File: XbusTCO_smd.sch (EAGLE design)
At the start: 80 parts, among them IC1 74HC4515D, IC2 PIC16F628P, IC3 MAX481CSA, IC4 78L05SMD, X1 1751264

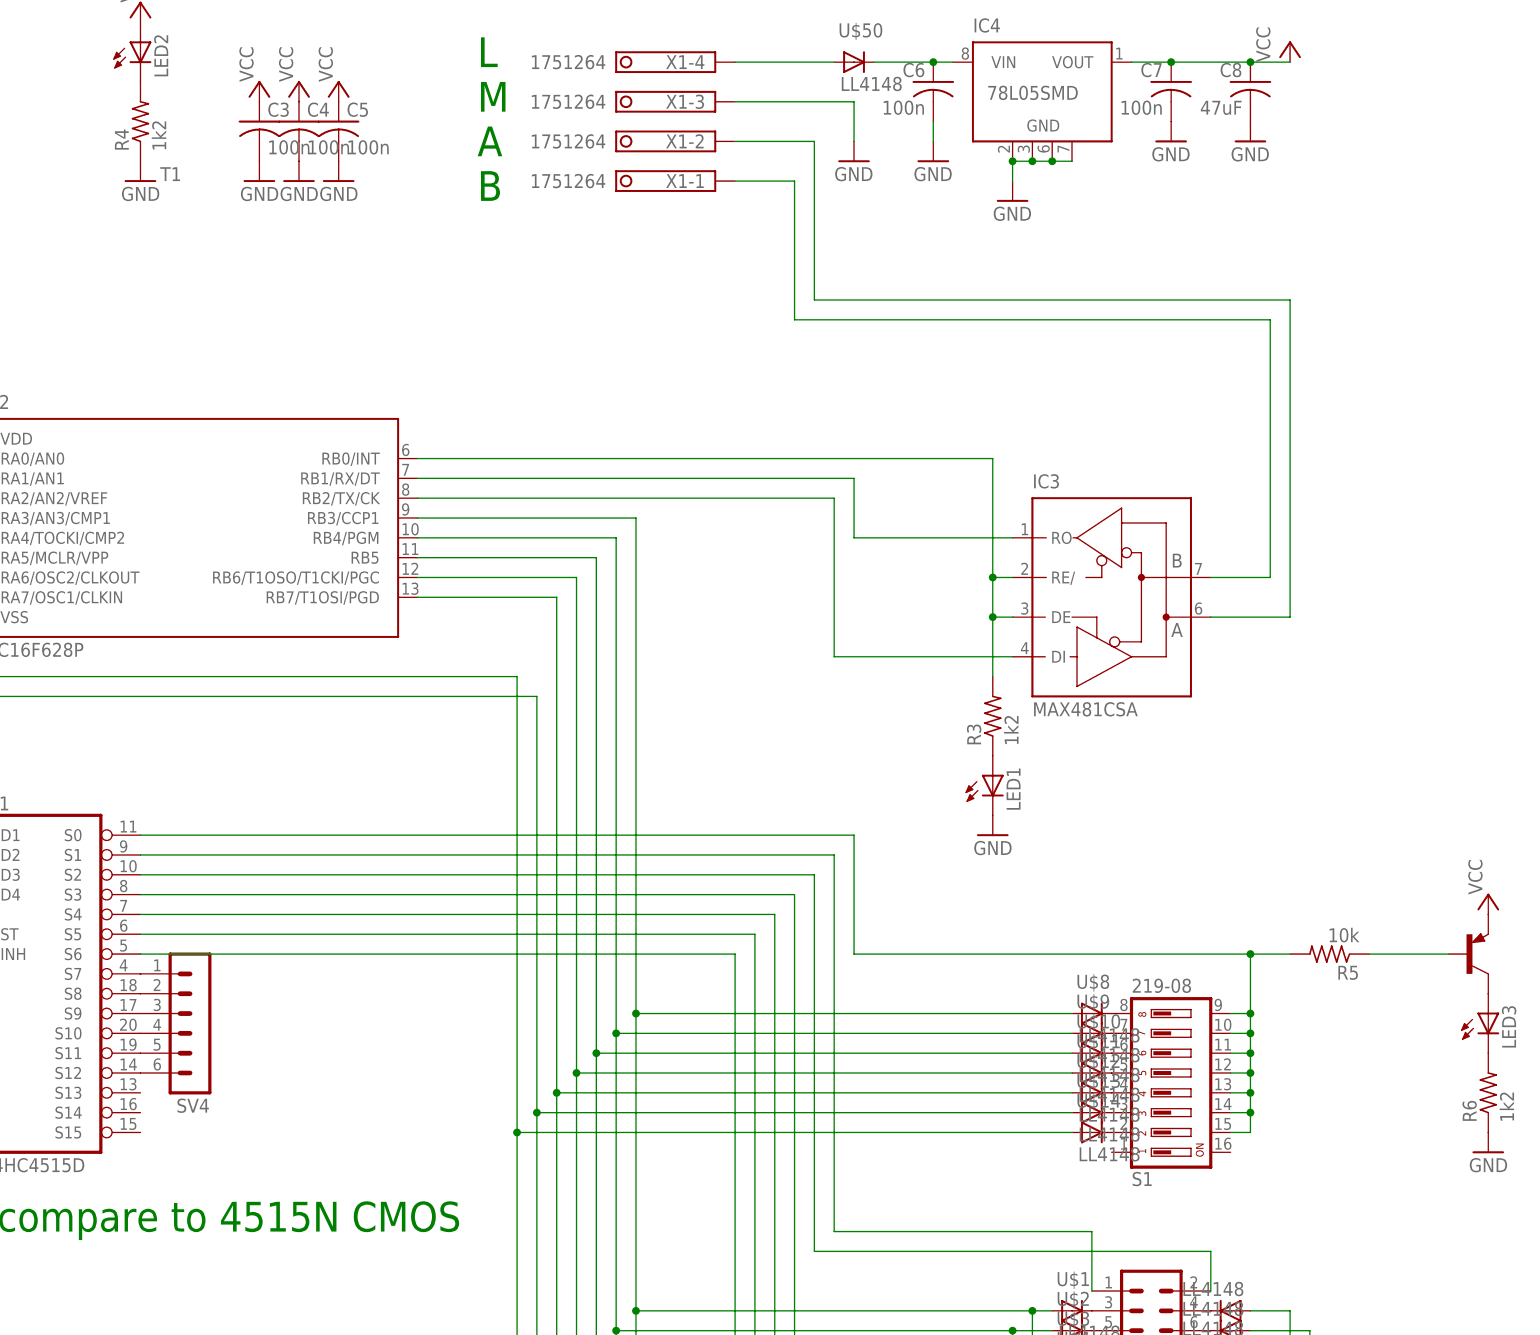
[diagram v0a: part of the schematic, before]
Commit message: Updated DIL switch pinout.
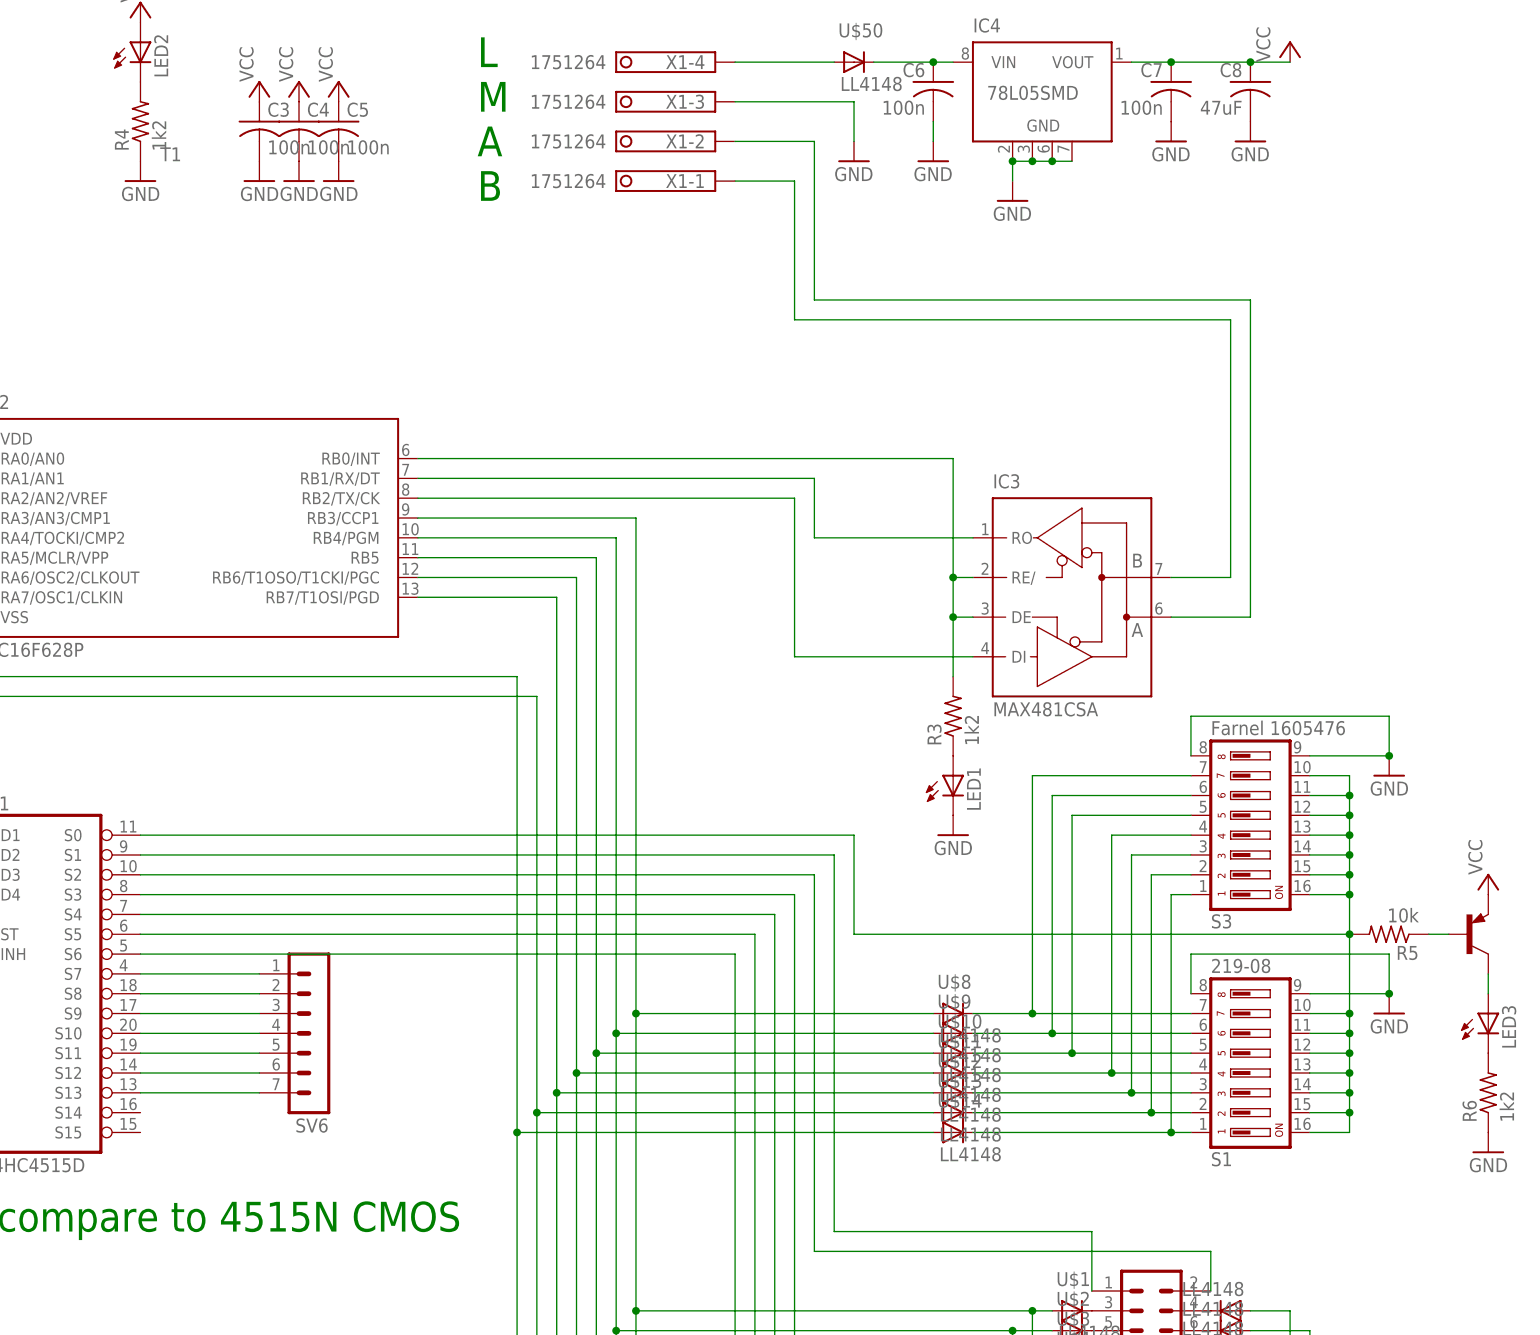
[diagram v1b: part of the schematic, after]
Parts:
- removed SV4: (no value), con-lstb:MA06-1
- added S3: Farnel 1605476, switch-dil:219-08J
- added SV6: (no value), con-lstb:MA07-1
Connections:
- new net N$88: IC1A.S13, SV6.7
- net GND: now also S1.8, S1.9, S3.8, S3.9
- net N$30: now also S1.16, S3.10, S3.11, S3.12, S3.13, S3.14, S3.15, S3.16; no longer S1.9
- net N$31: now also S1.7, S3.7; no longer S1.8
- net N$32: now also S1.6, S3.6; no longer S1.7
- net N$33: now also S1.5, S3.5; no longer S1.6
- net N$34: now also S1.4, S3.4; no longer S1.5
- net N$35: now also S1.3, S3.3; no longer S1.4
- net N$36: now also S1.2, S3.2; no longer S1.3
- net N$37: now also S1.1, S3.1; no longer S1.2
- net N$82: now also SV6.1; no longer SV4.1
- net N$83: now also SV6.2; no longer SV4.2
- net N$84: now also SV6.3; no longer SV4.3
- net N$85: now also SV6.4; no longer SV4.4
- net N$86: now also SV6.5; no longer SV4.5
- net N$87: now also SV6.6; no longer SV4.6
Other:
- moved on the sheet: IC3, LED1, R3, R5, S1, T1, U$10, U$11, U$12, U$13, U$14, U$8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

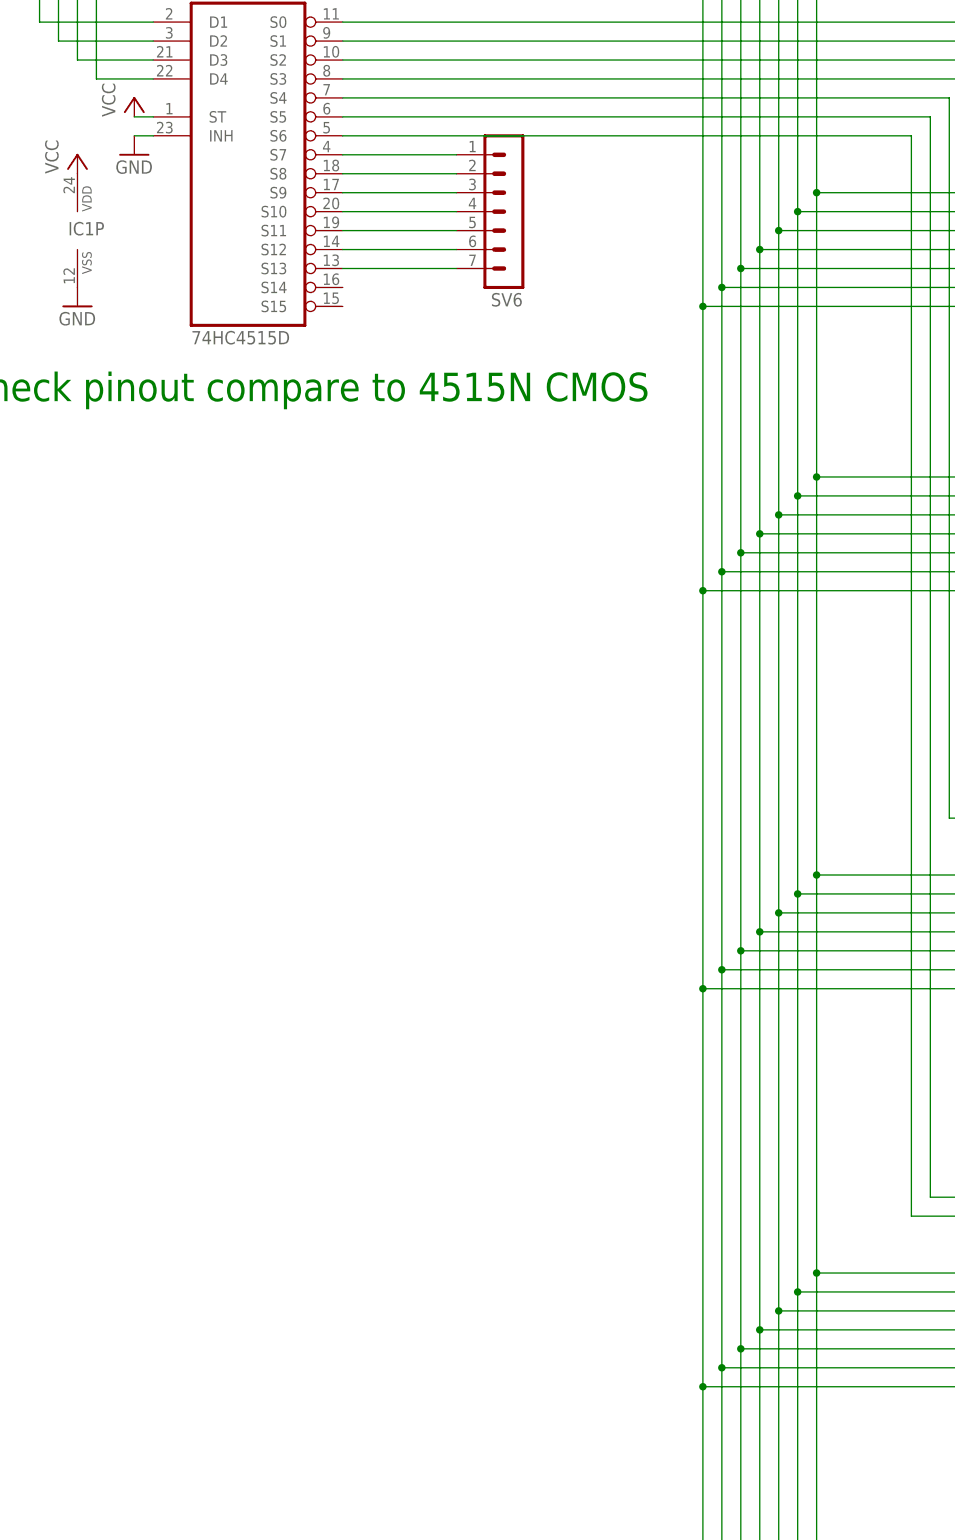
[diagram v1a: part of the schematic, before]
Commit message: Added 2 more connectors.
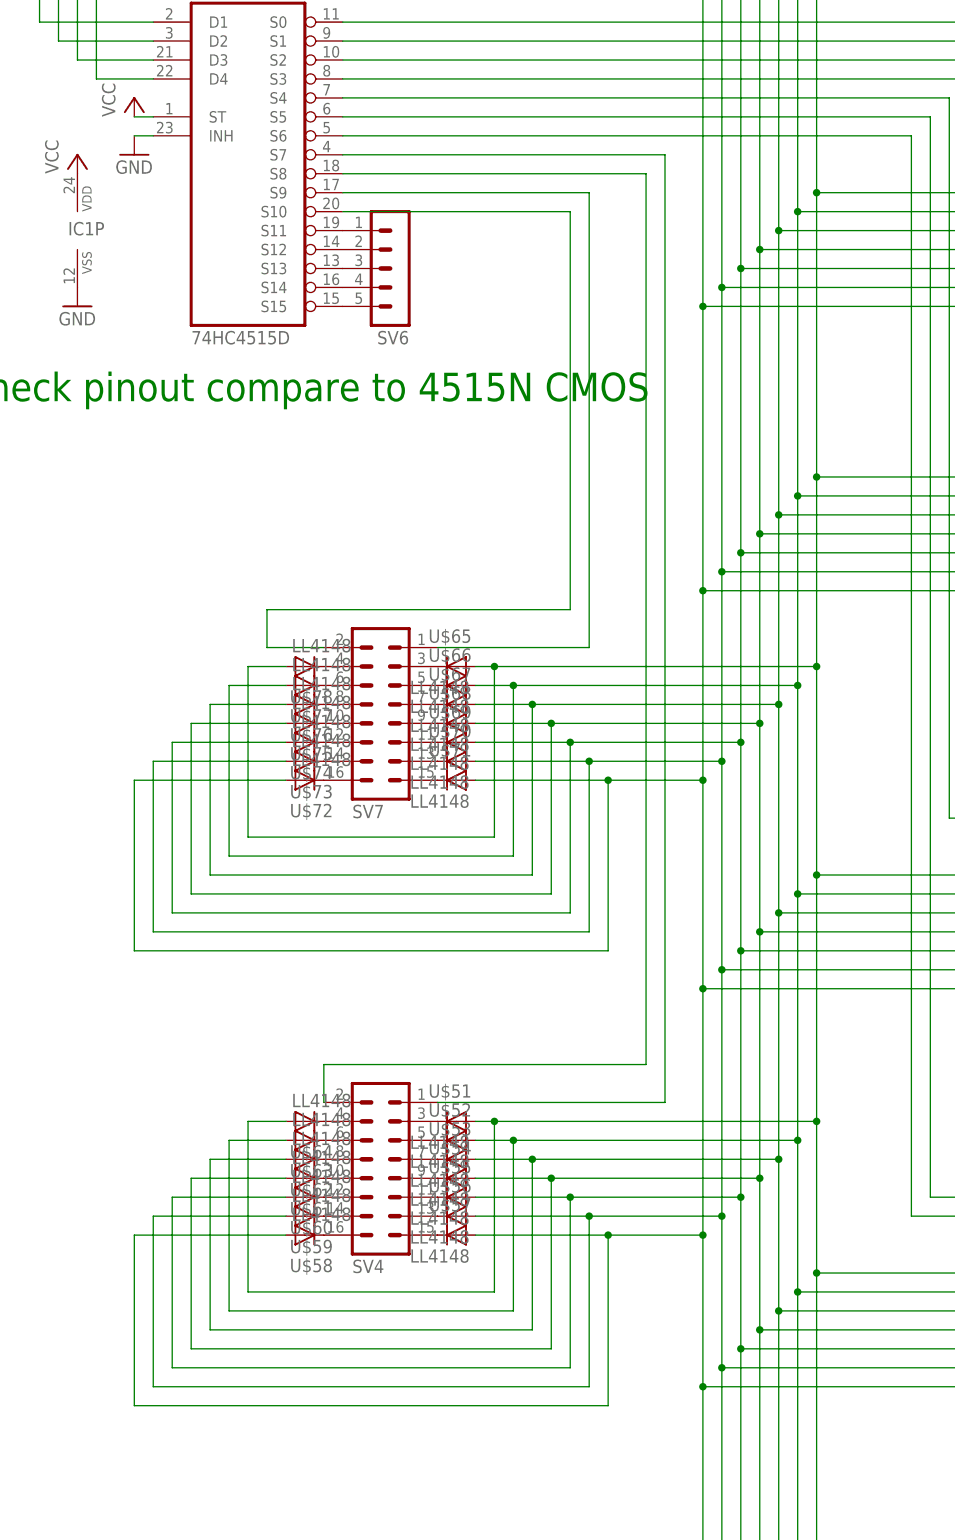
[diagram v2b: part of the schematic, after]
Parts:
- added SV4, SV7: (no value), con-lstb:MA08-2W
- added U$51, U$52, U$53, U$54, U$55, U$56, U$57, U$58, U$59, U$60, U$61, U$62, U$63, U$64, U$65, U$66, U$67, U$68, U$69, U$70, U$71, U$72, U$73, U$74, U$75, U$76, U$77, U$78: LL4148, LL4148:LL4148
- SV6: device con-lstb:MA07-1 -> con-lstb:MA05-1
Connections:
- new net N$100: SV4.7, U$53.C
- new net N$101: SV4.9, U$54.C
- new net N$102: SV4.11, U$55.C
- new net N$103: SV4.13, U$56.C
- new net N$104: SV4.15, U$57.C
- new net N$105: SV4.16, U$58.C
- new net N$106: SV4.14, U$59.C
- new net N$107: SV4.12, U$60.C
- new net N$108: SV4.10, U$61.C
- new net N$109: SV4.8, U$62.C
- new net N$110: SV4.6, U$63.C
- new net N$111: SV4.4, U$64.C
- new net N$112: SV7.7, U$67.C
- new net N$113: SV7.9, U$68.C
- new net N$114: SV7.11, U$69.C
- new net N$115: SV7.13, U$70.C
- new net N$116: SV7.15, U$71.C
- new net N$117: SV7.16, U$72.C
- new net N$118: SV7.14, U$73.C
- new net N$119: SV7.12, U$74.C
- new net N$120: SV7.10, U$75.C
- new net N$121: SV7.8, U$76.C
- new net N$122: SV7.6, U$77.C
- new net N$123: SV7.4, U$78.C
- new net N$89: IC1A.S14, SV6.4
- new net N$90: IC1A.S15, SV6.5
- new net N$96: SV7.3, U$65.C
- new net N$97: SV7.5, U$66.C
- new net N$98: SV4.3, U$51.C
- new net N$99: SV4.5, U$52.C
- net N$10: now also U$51.A, U$64.A, U$65.A, U$78.A
- net N$11: now also U$52.A, U$63.A, U$66.A, U$77.A
- net N$12: now also U$53.A, U$62.A, U$67.A, U$76.A
- net N$13: now also U$54.A, U$61.A, U$68.A, U$75.A
- net N$14: now also U$55.A, U$60.A, U$69.A, U$74.A
- net N$15: now also U$56.A, U$59.A, U$70.A, U$73.A
- net N$16: now also U$57.A, U$58.A, U$71.A, U$72.A
- net N$82: now also SV4.1; no longer SV6.1
- net N$83: now also SV4.2; no longer SV6.2
- net N$84: now also SV7.1; no longer SV6.3
- net N$85: now also SV7.2; no longer SV6.4
- net N$86: now also SV6.1; no longer SV6.5
- net N$87: now also SV6.2; no longer SV6.6
- net N$88: now also SV6.3; no longer SV6.7
